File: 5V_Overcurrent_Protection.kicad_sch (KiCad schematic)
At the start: 3 parts, among them U11 TPS2051CDBV

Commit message: Finalised RS485 Circuit, Layout improvemnts, mounting holes, silkscreen...
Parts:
- D24: LCSC (none) -> C2286
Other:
- company: (none) -> eChook
- title: (none) -> BMS Comms Master Board
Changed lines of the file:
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@@
 	(generator_version "9.0")
 	(paper "A4")
+	(title_block
+		(title "BMS Comms Master Board")
+		(date "2025-05-21")
+		(rev "0.1")
+		(company "eChook")
+	)
 	(rectangle
 		(start 114.3 53.34)
@@
 					(unit 1)
 				)
-				(path "/d7e219ab-f530-45f5-8a23-0e6b6d2e3e0f/9d93b8a4-aa8b-48c1-bfa0-dc1a7f04dbe5"
-					(reference "U17")
-					(unit 1)
-				)
 				(path "/d7e219ab-f530-45f5-8a23-0e6b6d2e3e0f/c3056ab1-5cdf-4364-9ad2-3f439474eb1e"
 					(reference "U12")
@@
 				(path "/d7e219ab-f530-45f5-8a23-0e6b6d2e3e0f/29683fdb-af89-4404-82da-8f039745472d"
 					(reference "R31")
-					(unit 1)
-				)
-				(path "/d7e219ab-f530-45f5-8a23-0e6b6d2e3e0f/9d93b8a4-aa8b-48c1-bfa0-dc1a7f04dbe5"
-					(reference "R61")
 					(unit 1)
 				)
@@
 			)
 		)
-		(property "LCSC" ""
+		(property "LCSC" "C2286"
 			(at 185.42 85.09 90)
 			(effects
@@
 					(unit 1)
 				)
-				(path "/d7e219ab-f530-45f5-8a23-0e6b6d2e3e0f/9d93b8a4-aa8b-48c1-bfa0-dc1a7f04dbe5"
-					(reference "D43")
-					(unit 1)
-				)

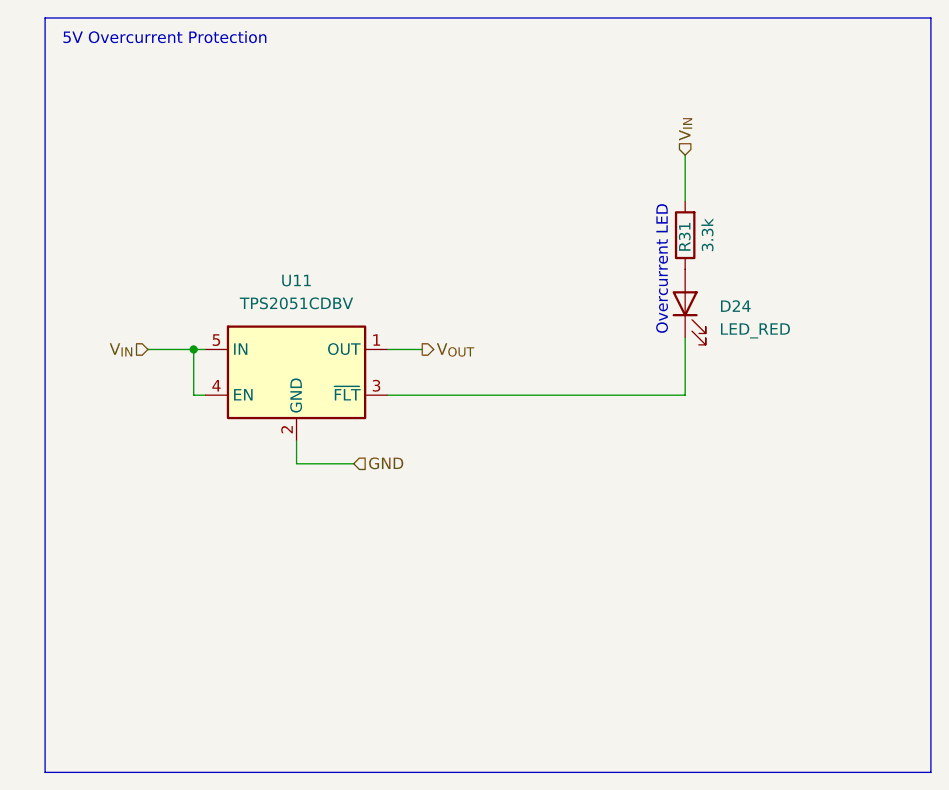
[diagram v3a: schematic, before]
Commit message: Implemented schematic review suggestions (Notes.txt)
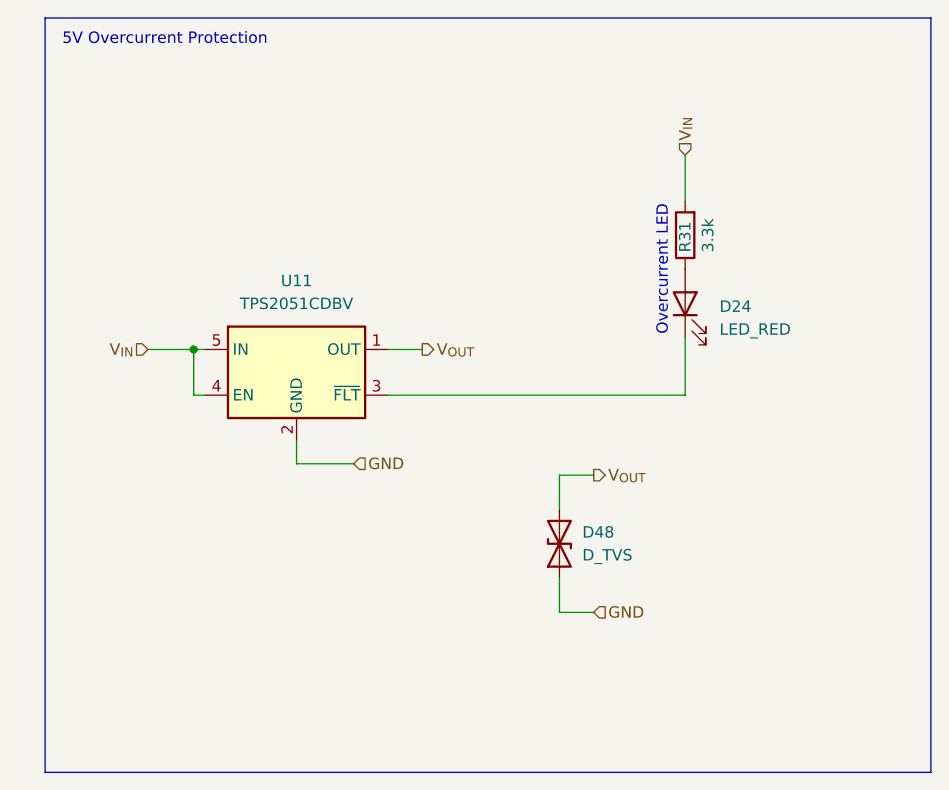
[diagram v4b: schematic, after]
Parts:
- added D48: D_TVS, Diode_SMD:D_SOD-523, symbol Device:D_TVS
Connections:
- net GND: now also D48.1 (A1)
- net V_{OUT}: now also D48.2 (A2)
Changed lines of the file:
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@@
+	(wire
+		(pts
+			(xy 171.45 119.38) (xy 171.45 115.57)
+		)
+		(stroke
+			(width 0)
+			(type default)
+		)
+	)
 	(wire
 		(pts
@@
 	(wire
 		(pts
+			(xy 175.26 119.38) (xy 171.45 119.38)
+		)
+		(stroke
+			(width 0)
+			(type default)
+		)
+	)
+	(wire
+		(pts
+			(xy 175.26 104.14) (xy 171.45 104.14)
+		)
+		(stroke
+			(width 0)
+			(type default)
+		)
+	)
+	(wire
+		(pts
 			(xy 142.24 102.87) (xy 148.59 102.87)
 		)
@@
 		(pts
 			(xy 152.4 90.17) (xy 156.21 90.17)
+		)
+		(stroke
+			(width 0)
+			(type default)
+		)
+	)
+	(wire
+		(pts
+			(xy 171.45 104.14) (xy 171.45 107.95)
 		)
 		(stroke
@@
 		(shape input)
 		(at 148.59 102.87 0)
+		(effects
+			(font
+				(size 1.27 1.27)
+			)
+			(justify left)
+		)
+	)
+	(hierarchical_label "GND"
+		(shape input)
+		(at 175.26 119.38 0)
+		(effects
+			(font
+				(size 1.27 1.27)
+			)
+			(justify left)
+		)
+	)
+	(hierarchical_label "V_{OUT}"
+		(shape output)
+		(at 175.26 104.14 0)
 		(effects
 			(font
@@
 					(unit 1)
 				)
+			)
+		)
+	)
+	(symbol
+		(lib_id "Device:D_TVS")
+		(at 171.45 111.76 90)
+		(unit 1)
+		(exclude_from_sim no)
+		(in_bom yes)
+		(on_board yes)
+		(dnp no)
+		(fields_autoplaced yes)
+		(property "Reference" "D48"
+			(at 173.99 110.4899 90)
+			(effects
+				(font
+					(size 1.27 1.27)
+				)
+				(justify right)
+			)
+		)
+		(property "Value" "D_TVS"
+			(at 173.99 113.0299 90)
+			(effects
+				(font
+					(size 1.27 1.27)
+				)
+				(justify right)
+			)
+		)
+		(property "Footprint" "Diode_SMD:D_SOD-523"
+			(at 171.45 111.76 0)
+			(effects
+				(font
+					(size 1.27 1.27)
+				)
+				(hide yes)
+			)
+		)
+		(property "Datasheet" "~"
+			(at 171.45 111.76 0)
+			(effects
+				(font
+					(size 1.27 1.27)
+				)
+				(hide yes)
+			)
+		)
+		(property "Description" "Bidirectional transient-voltage-suppression diode"
+			(at 171.45 111.76 0)
+			(effects
+				(font
+					(size 1.27 1.27)
+				)
+				(hide yes)
+			)
+		)
+		(property "LCSC" "C477993"
+			(at 171.45 111.76 90)
+			(effects
+				(font
+					(size 1.27 1.27)
+				)
+				(hide yes)
+			)
+		)
+		(pin "1"
+		)
+		(pin "2"
+		)
+		(instances
+			(project ""
+				(path "/d7e219ab-f530-45f5-8a23-0e6b6d2e3e0f/29683fdb-af89-4404-82da-8f039745472d"
+					(reference "D48")
+					(unit 1)
+				)
+				(path "/d7e219ab-f530-45f5-8a23-0e6b6d2e3e0f/c3056ab1-5cdf-4364-9ad2-3f439474eb1e"
+					(reference "D50")
+					(unit 1)
+				)
+				(path "/d7e219ab-f530-45f5-8a23-0e6b6d2e3e0f/edb12572-d726-408e-abc9-877ec2f4dc08"
+					(reference "D49")
+					(unit 1)
+				)
+				(path "/d7e219ab-f530-45f5-8a23-0e6b6d2e3e0f/f3360caf-e324-45d1-b704-f30b29e9918c"
+					(reference "D51")
+					(unit 1)
+				)

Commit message: Added 5V protection capacitors, altered 5V_ISO Output Caps, Corrected RX<>TX for Serial3
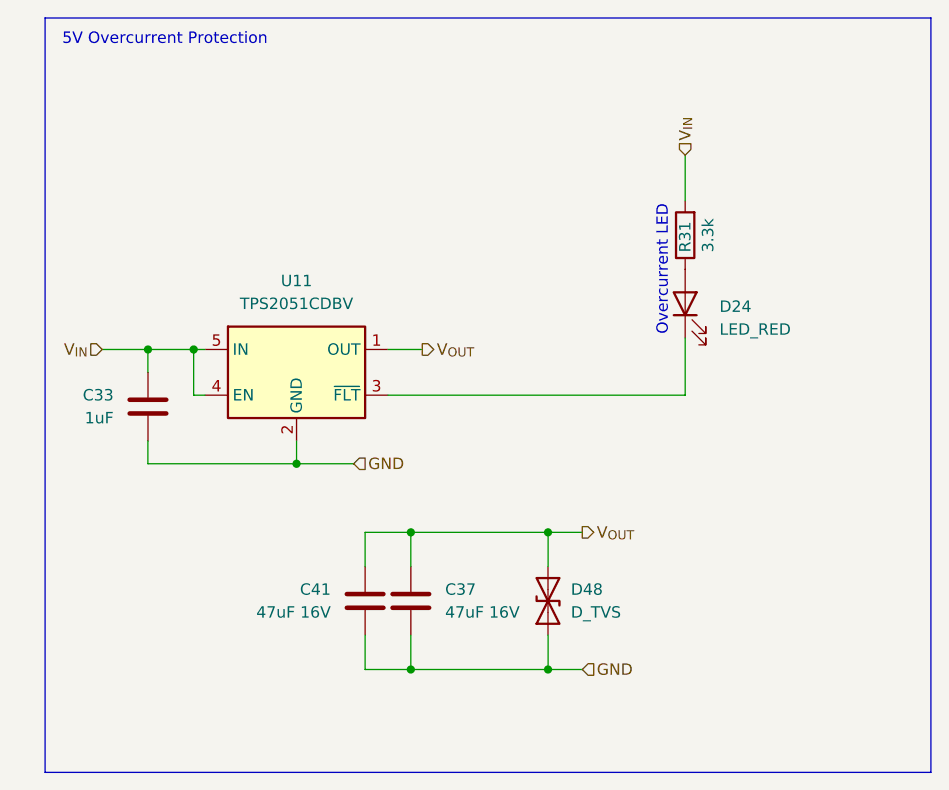
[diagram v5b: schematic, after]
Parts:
- added C33: 1uF, Capacitor_SMD:C_0603_1608Metric, symbol Device:C
- added C37, C41: 47uF 16V, Capacitor_SMD:C_1210_3225Metric, symbol Device:C
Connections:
- net GND: now also C33.2, C37.2, C41.2
- net V_{IN}: now also C33.1
- net V_{OUT}: now also C37.1, C41.1
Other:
- moved on the sheet: D48

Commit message: Added pulldown safety resistors, layout improvements
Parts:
- D48: Manufacturer (none) -> Nexperia
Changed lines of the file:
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@@
 			)
 		)
-		(property "Datasheet" "~"
+		(property "Datasheet" "https://lcsc.com/datasheet/lcsc_datasheet_2410122007_Nexperia-PESD5V0V1BB-115_C477993.pdf"
 			(at 170.18 118.11 0)
 			(effects
@@
 			)
 		)
-		(property "Description" "Bidirectional transient-voltage-suppression diode"
+		(property "Description" "Bidirectional TVS Diode, Nexperia PESD5V0V1BB,115"
 			(at 170.18 118.11 0)
 			(effects
@@
 			(at 170.18 118.11 90)
 			(effects
+				(font
+					(size 1.27 1.27)
+				)
+				(hide yes)
+			)
+		)
+		(property "Manufacturer" "Nexperia"
+			(at 170.18 118.11 90)
+			(effects
